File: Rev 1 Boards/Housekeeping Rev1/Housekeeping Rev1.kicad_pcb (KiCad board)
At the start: 2 copper layers, 54 parts, among them J1 Conn_01x02_Socket, J2 Conn_01x02_Socket, J3 Conn_01x02_Socket, J4 Conn_01x02_Socket, J5 Conn_01x02_Socket, J6 Conn_01x02_Socket, U1 MC34063A, U2 MC34063A, U3 MC34063A, U4 MC34063A

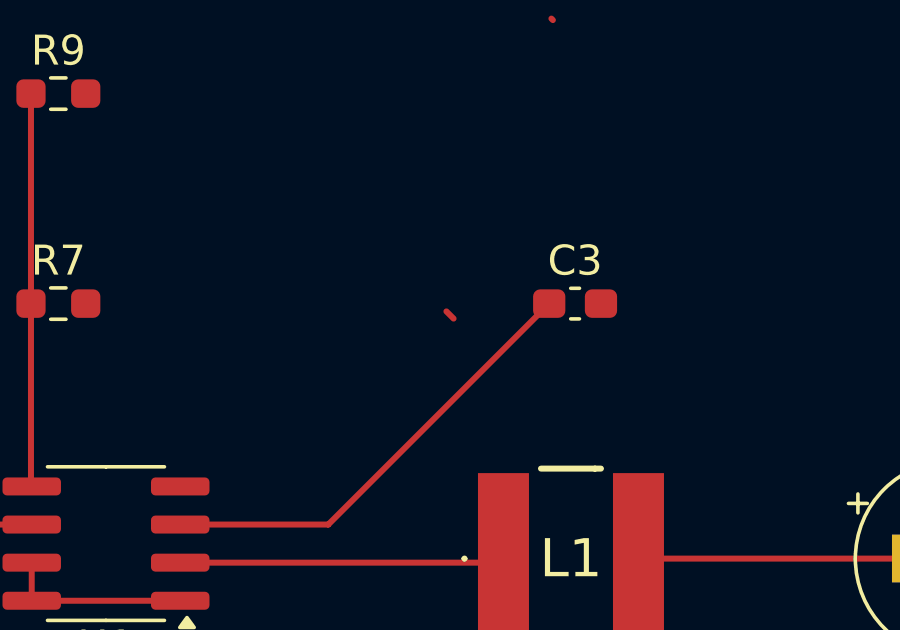
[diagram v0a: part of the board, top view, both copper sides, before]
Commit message: added mouser part numbers and corresponding datasheets/footprints for components
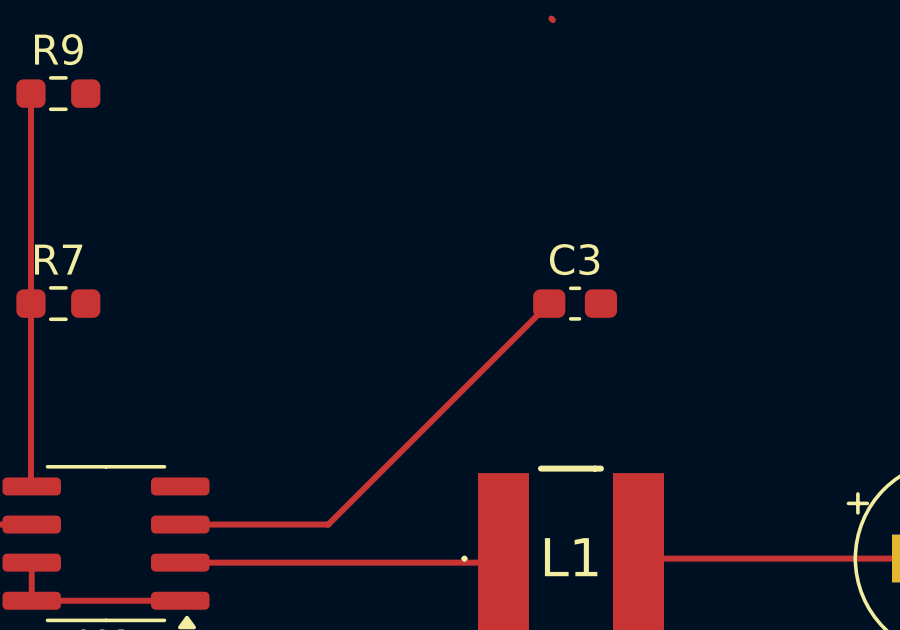
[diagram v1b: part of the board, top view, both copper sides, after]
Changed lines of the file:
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@@
-	)
-	(segment
-		(start 83.347349 149.759849)
-		(end 83.5875 150)
-		(width 0.2)
-		(layer "F.Cu")
-		(net 16)
 	)
 	(segment

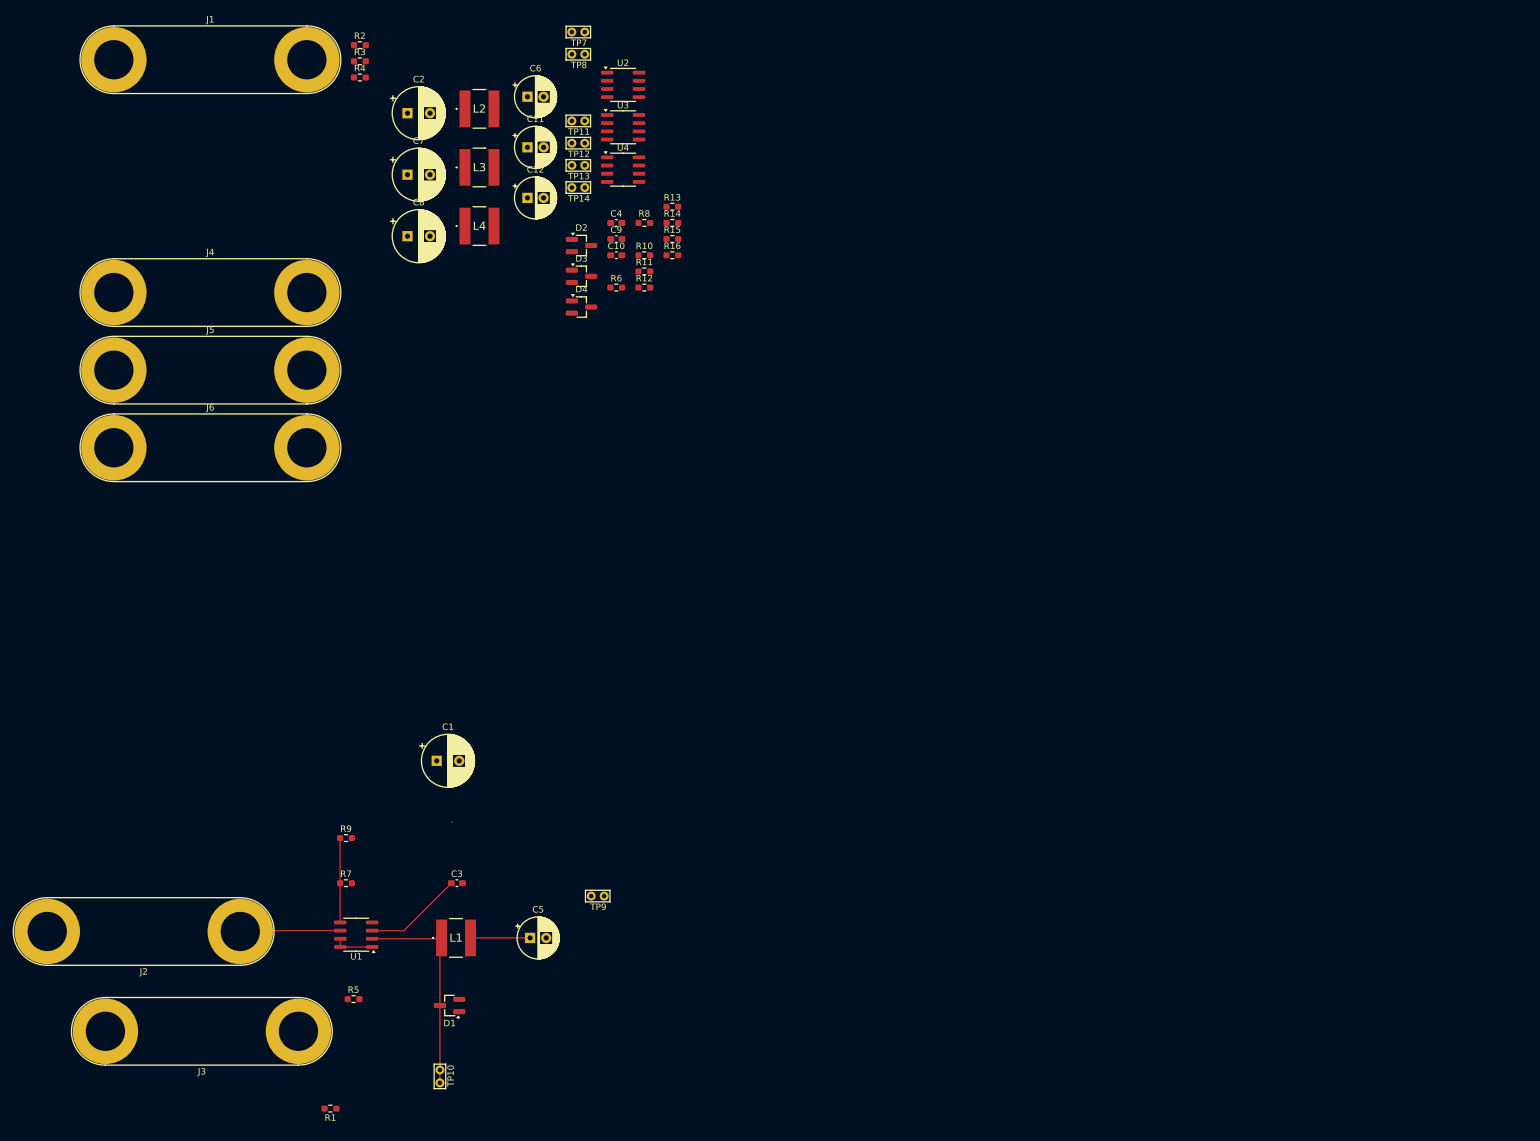
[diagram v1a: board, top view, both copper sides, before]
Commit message: began pcb layout ofr housekeeping
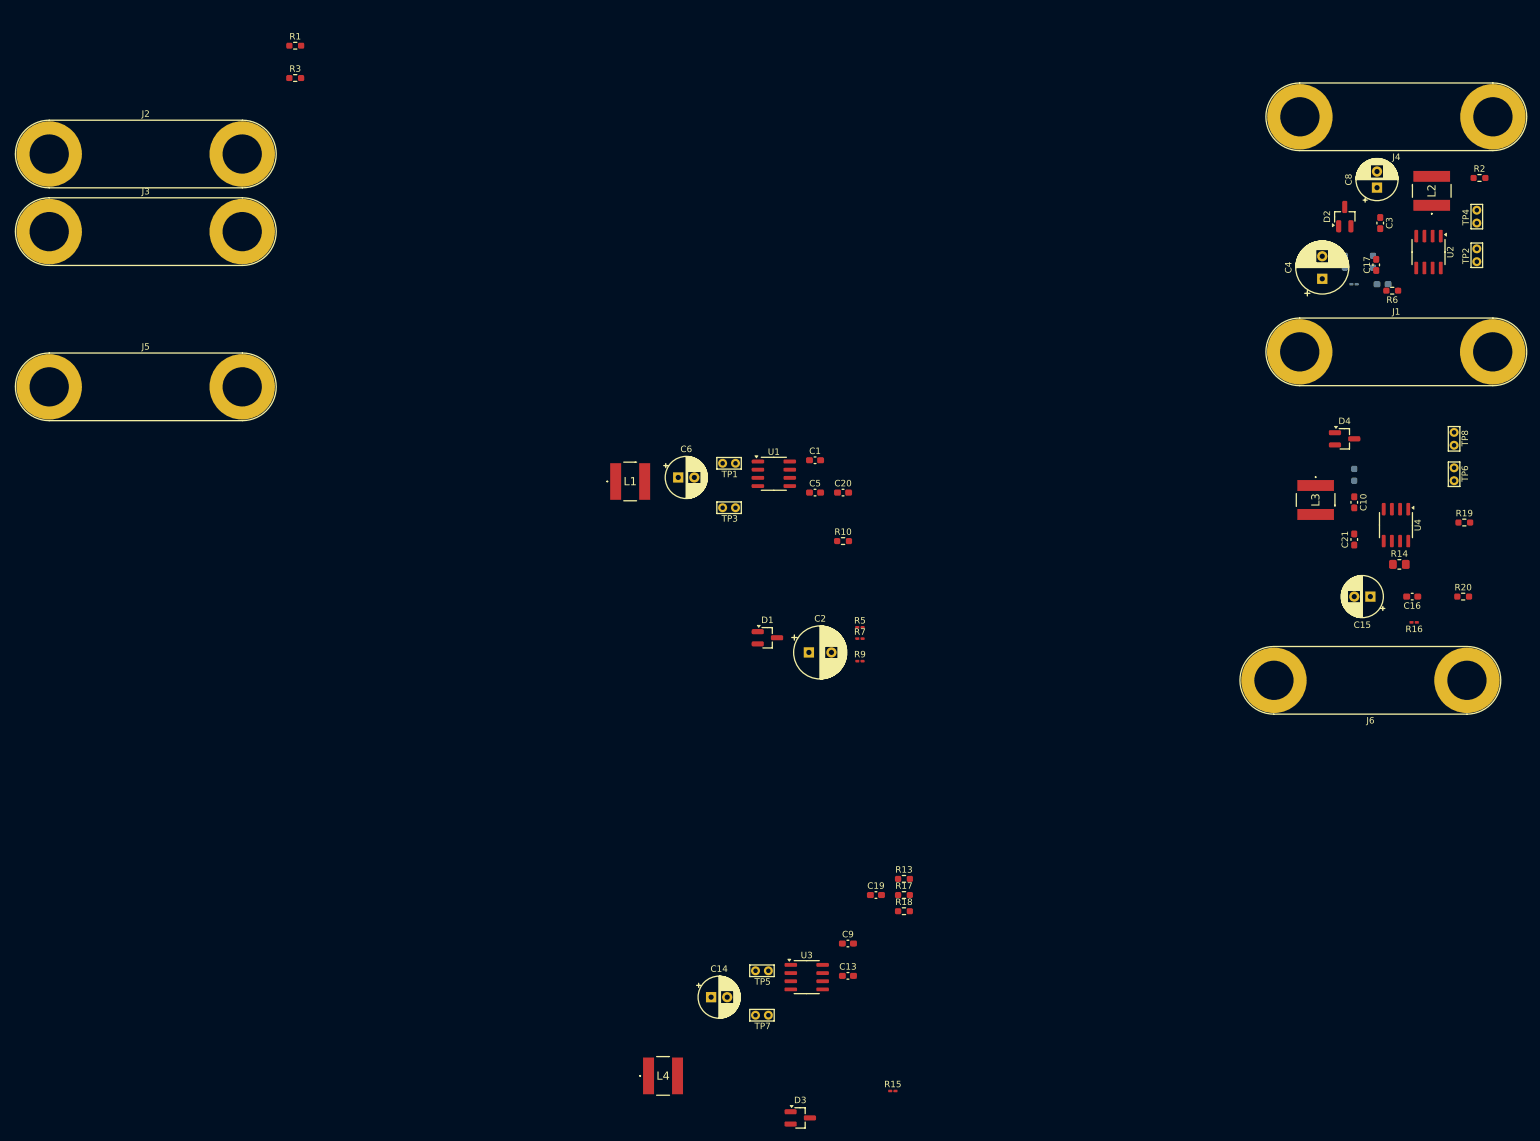
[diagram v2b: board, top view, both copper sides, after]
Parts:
- removed C11, C12: 470u, Capacitor_THT:CP_Radial_D6.3mm_P2.50mm
- removed TP10, TP12, TP14: V_{E}, TestPoint:TestPoint_Bridge_Pitch2.0mm_Drill0.7mm
- removed TP11, TP13, TP9: V_{C}, TestPoint:TestPoint_Bridge_Pitch2.0mm_Drill0.7mm
- added C13: 0.01u, Capacitor_SMD:C_0603_1608Metric_Pad1.08x0.95mm_HandSolder, F.Cu at (148.3, 163.9)
- added C14: 470u, Capacitor_THT:CP_Radial_D6.3mm_P2.50mm, F.Cu at (127.1, 167.2)
- added C15: 470u, Capacitor_THT:CP_Radial_D6.3mm_P2.50mm, F.Cu at (229.5, 105.0)
- added C16: 0.01u, Capacitor_SMD:C_0603_1608Metric_Pad1.08x0.95mm_HandSolder, F.Cu at (236.0, 105.0)
- added C17: 1u, Capacitor_SMD:C_0603_1608Metric_Pad1.08x0.95mm_HandSolder, F.Cu at (230.4, 53.5)
- added C19: 1u, Capacitor_SMD:C_0603_1608Metric_Pad1.08x0.95mm_HandSolder, F.Cu at (152.7, 151.3)
- added C20: 1u, Capacitor_SMD:C_0603_1608Metric_Pad1.08x0.95mm_HandSolder, F.Cu at (147.6, 88.8)
- added C21: 1u, Capacitor_SMD:C_0603_1608Metric_Pad1.08x0.95mm_HandSolder, F.Cu at (227.0, 96.1)
- added R17: 12k, Resistor_SMD:R_0603_1608Metric_Pad0.98x0.95mm_HandSolder, F.Cu at (157.1, 151.3)
- added R18: 1.8k, Resistor_SMD:R_0603_1608Metric_Pad0.98x0.95mm_HandSolder, F.Cu at (157.1, 153.8)
- added R19: 6.8k, Resistor_SMD:R_0603_1608Metric_Pad0.98x0.95mm_HandSolder, F.Cu at (244.1, 93.5)
- added R20: 820, Resistor_SMD:R_0603_1608Metric_Pad0.98x0.95mm_HandSolder, F.Cu at (243.9, 105.0)
- added TP1: V_{C}, TestPoint:TestPoint_Bridge_Pitch2.0mm_Drill0.7mm, F.Cu at (128.9, 84.3)
- added TP2: V_{C}, TestPoint:TestPoint_Bridge_Pitch2.0mm_Drill0.7mm, F.Cu at (246.0, 51.0)
- added TP3: V_{E}, TestPoint:TestPoint_Bridge_Pitch2.0mm_Drill0.7mm, F.Cu at (128.9, 91.2)
- added TP4: V_{E}, TestPoint:TestPoint_Bridge_Pitch2.0mm_Drill0.7mm, F.Cu at (246.0, 45.0)
- added TP5: V_{C}, TestPoint:TestPoint_Bridge_Pitch2.0mm_Drill0.7mm, F.Cu at (134.0, 163.1)
- added TP6: V_{C}, TestPoint:TestPoint_Bridge_Pitch2.0mm_Drill0.7mm, F.Cu at (242.5, 87.0)
- C1: value 100u -> 75p; footprint Capacitor_THT:CP_Radial_D8.0mm_P3.50mm -> Capacitor_SMD:C_0603_1608Metric_Pad1.08x0.95mm_HandSolder
- C10: value 470p -> 68p
- C3: value 470p -> 75p
- C4: value 470p -> 100u; footprint Capacitor_SMD:C_0603_1608Metric_Pad1.08x0.95mm_HandSolder -> Capacitor_THT:CP_Radial_D8.0mm_P3.50mm
- C5: value 470u -> 0.01u; footprint Capacitor_THT:CP_Radial_D6.3mm_P2.50mm -> Capacitor_SMD:C_0603_1608Metric_Pad1.08x0.95mm_HandSolder
- C7: value 100u -> 0.01u; footprint Capacitor_THT:CP_Radial_D8.0mm_P3.50mm -> Capacitor_SMD:C_0603_1608Metric_Pad1.08x0.95mm_HandSolder; moved to B.Cu
- C8: value 100u -> 470u; footprint Capacitor_THT:CP_Radial_D8.0mm_P3.50mm -> Capacitor_THT:CP_Radial_D6.3mm_P2.50mm
- C9: value 470p -> 100p
- R10: value 3.6k -> 820
- R11: value 0.33 -> 6.8k; moved to B.Cu
- R12: value 0.24 -> 820; moved to B.Cu
- R13: value 2.2k -> 1
- R14: value 3.6k -> 0.866; footprint Resistor_SMD:R_0603_1608Metric_Pad0.98x0.95mm_HandSolder -> Resistor_SMD:R_0805_2012Metric_Pad1.20x1.40mm_HandSolder
- R15: value 3.6k -> 4.7k; footprint Resistor_SMD:R_0603_1608Metric_Pad0.98x0.95mm_HandSolder -> Resistor_SMD:R_0201_0603Metric_Pad0.64x0.40mm_HandSolder
- R16, R7: value 2.2k -> 1.2k; footprint Resistor_SMD:R_0603_1608Metric_Pad0.98x0.95mm_HandSolder -> Resistor_SMD:R_0201_0603Metric_Pad0.64x0.40mm_HandSolder
- R4: moved to B.Cu
- R5: value 0.33 -> 1; footprint Resistor_SMD:R_0603_1608Metric_Pad0.98x0.95mm_HandSolder -> Resistor_SMD:R_0201_0603Metric_Pad0.64x0.40mm_HandSolder
- R6: value 0.33 -> 1
- R8: footprint Resistor_SMD:R_0603_1608Metric_Pad0.98x0.95mm_HandSolder -> Resistor_SMD:R_0201_0603Metric_Pad0.64x0.40mm_HandSolder; moved to B.Cu
- R9: value 3.6k -> 6.8k; footprint Resistor_SMD:R_0603_1608Metric_Pad0.98x0.95mm_HandSolder -> Resistor_SMD:R_0201_0603Metric_Pad0.64x0.40mm_HandSolder
- TP7: value V_{C} -> V_{E}
- moved J4 215.9 mm to (248.5, 30.5), turned to 180 degrees
- moved J6 213.2 mm to (244.5, 118.0), turned to 180 degrees
- moved J1 189.6 mm to (218.5, 67.0)
- moved C3 176.2 mm to (231.0, 47.0), turned to -90 degrees
- moved R2 175.1 mm to (246.4, 40.0)
- moved R4 166.3 mm to (227.0, 86.1), turned to -90 degrees
- moved R1 165.1 mm to (62.5, 19.5), turned to 0 degrees
- moved TP7 155.3 mm to (134.0, 170.0)
- moved C7 152.4 mm to (231.4, 56.5), turned to 180 degrees
- moved C8 150.7 mm to (230.5, 41.5), turned to 90 degrees
- moved TP8 149.8 mm to (242.5, 81.5), turned to 90 degrees
- moved L2 148.4 mm to (239.0, 42.0), turned to 90 degrees
- moved L3 139.7 mm to (221.0, 90.0), turned to -90 degrees
- moved R15 136.6 mm to (155.3, 181.8)
- moved D3 135.0 mm to (140.9, 185.9)
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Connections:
- C1 pad 1: /+24_{MiniPC} -> Net-(U1-CT)
- C3 pad 1: Net-(U1-CT) -> Net-(U2-CT)
- C4 pad 1: Net-(U2-CT) -> +24V
- C5 pad 1: +3V3 -> Net-(U1-COMP-)
- C5 pad 2: GND -> +3V3
- C6 pad 1: +5V -> +3V3
- C7 pad 1: +24V -> Net-(U2-COMP-)
- C7 pad 2: GND -> +3.3VA
- C8 pad 1: /+24_{MiniPC} -> +3.3VA
- C8 pad 2: GND -> GNDPWR
- J4 pad 2: GND -> GNDPWR
- L2 pad 2: +5V -> +3.3VA
- L4 pad 2: +3.3VA -> +5V
- R10 pad 1: Net-(U2-COMP-) -> Net-(U1-COMP-)
- R10 pad 2: +5V -> GND
- R11 pad 1: +24V -> Net-(U2-COMP-)
- R11 pad 2: Net-(U3-DC) -> GND
- R12 pad 1: /+24_{MiniPC} -> Net-(U2-COMP-)
- R12 pad 2: Net-(U4-DC) -> GND
- R13 pad 1: Net-(U3-COMP-) -> /+24_{MiniPC}
- R13 pad 2: GNDPWR -> Net-(U3-DC)
- R14 pad 1: Net-(U4-COMP-) -> /+24_{MiniPC}
- R14 pad 2: GNDPWR -> Net-(U4-DC)
- R15 pad 2: +3.3VA -> +5V
- R6 pad 1: /+24_{MiniPC} -> +24V
- R7 pad 2: GND -> +3V3
- R8 pad 1: Net-(U2-COMP-) -> +3.3VA
- R8 pad 2: GND -> Net-(U2-COMP-)
- R9 pad 2: +3V3 -> GND
- TP7 pad 1: Net-(U2-DC) -> Net-(D3-K)
- TP8 pad 1: Net-(D2-K) -> Net-(D4-K)
- U2 pad 6: /+24_{MiniPC} -> +24V
- U3 pad 6: +24V -> /+24_{MiniPC}
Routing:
- net Net-(D1-K): track 33.4 -> 0.00 mm
- net /+24_{MiniPC}: track 15.6 -> 0.00 mm
- net Net-(U1-CT): track 15.5 -> 0.00 mm
- net Net-(U1-COMP-): track 13.1 -> 0.00 mm
- net +3V3: track 9.25 -> 0.00 mm
- net Net-(U1-DC): track 6.22 -> 0.00 mm

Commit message: Created rudimentary component placements for Housekeeping PCB layout Pending approval from Jed before putting down traces
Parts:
- C1, C16, C9, D4, R13, R16, R17, R18, R19, R20: moved to B.Cu
- moved J2 180.3 mm to (203.0, 60.5), turned to 90 degrees
- moved J5 142.4 mm to (164.5, 97.5)
- moved J3 134.3 mm to (158.0, 61.0), turned to 90 degrees
- moved R3 119.6 mm to (164.5, 87.0), turned to -90 degrees
- moved D3 118.0 mm to (172.0, 72.2)
- moved R1 112.3 mm to (169.6, 53.5), turned to 180 degrees
- moved L4 112.2 mm to (170.5, 79.4), turned to -90 degrees
- moved R15 104.7 mm to (179.5, 80.0), turned to -90 degrees
- moved U3 97.9 mm to (180.0, 73.9)
- moved C14 91.9 mm to (170.5, 86.2), turned to -90 degrees
- moved TP5 91.7 mm to (157.5, 74.5), turned to 90 degrees
- moved C13 88.6 mm to (177.0, 80.0), turned to -90 degrees
- moved TP7 88.2 mm to (157.5, 85.0), turned to 90 degrees
- moved C9 86.4 mm to (173.2, 76.2), turned to 180 degrees
- moved C2 84.9 mm to (190.0, 43.5)
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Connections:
- C15 pad 1: GNDPWR -> GND
- C17 pad 2: GND -> GNDPWR
- C3 pad 2: GND -> GNDPWR
- C4 pad 2: GND -> GNDPWR
- D2 pad 1: GND -> GNDPWR
- R11 pad 2: GND -> GNDPWR
- R12 pad 2: GND -> GNDPWR
- R19 pad 2: GNDPWR -> GND
- R20 pad 2: GNDPWR -> GND
- U2 pad 4: GND -> GNDPWR
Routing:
- net Net-(U2-COMP-): vias 0 -> 1
- added copper zone on B.Cu, net GND
- added copper zone on B.Cu, net GNDPWR
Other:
- board outline added: 127 x 98 mm
